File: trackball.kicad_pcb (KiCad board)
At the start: 2 copper layers, 27.5 x 35.2 mm, 37 parts, among them P1 CONN_10, P2 CONN_5, U1 MKL03Z32VFK4, U2 ADNS-3530, U4 ESD

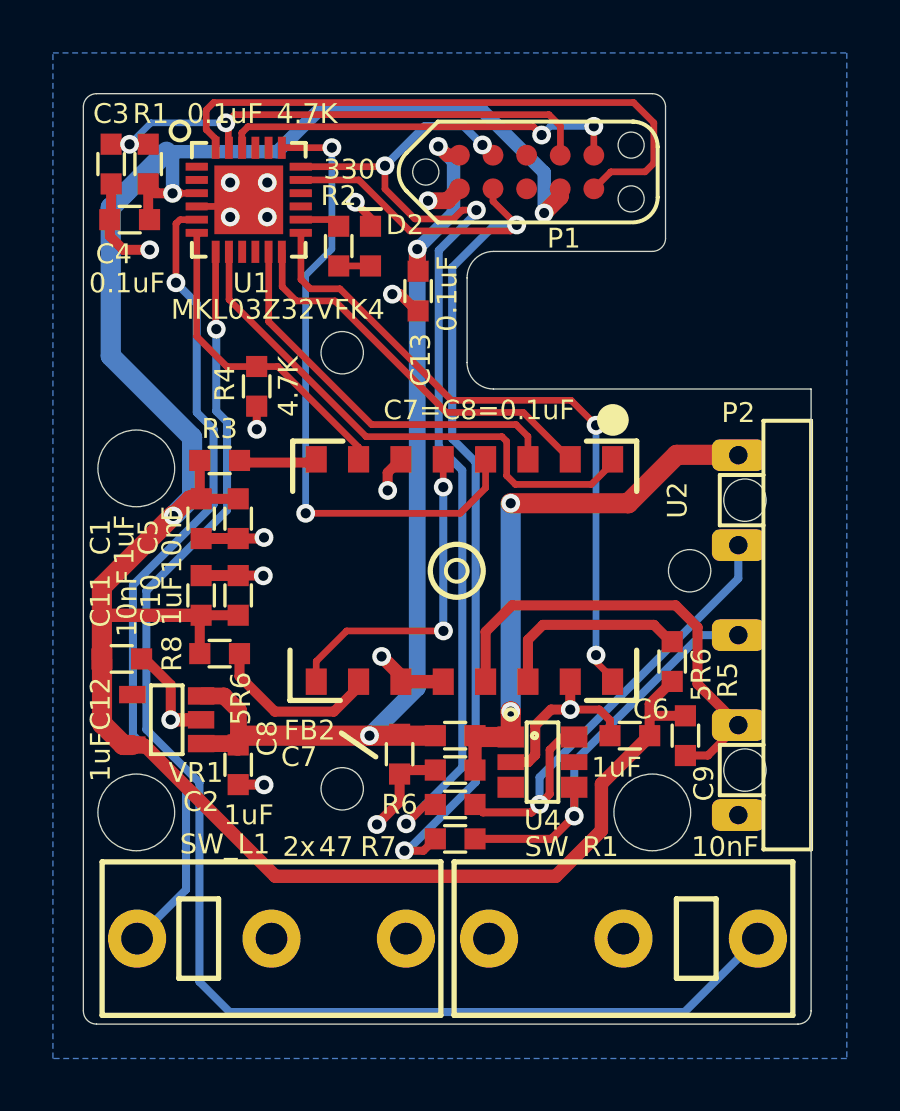
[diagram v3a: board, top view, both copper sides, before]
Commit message: Improve silk screen. Feature 5.6 instead of 5R6.
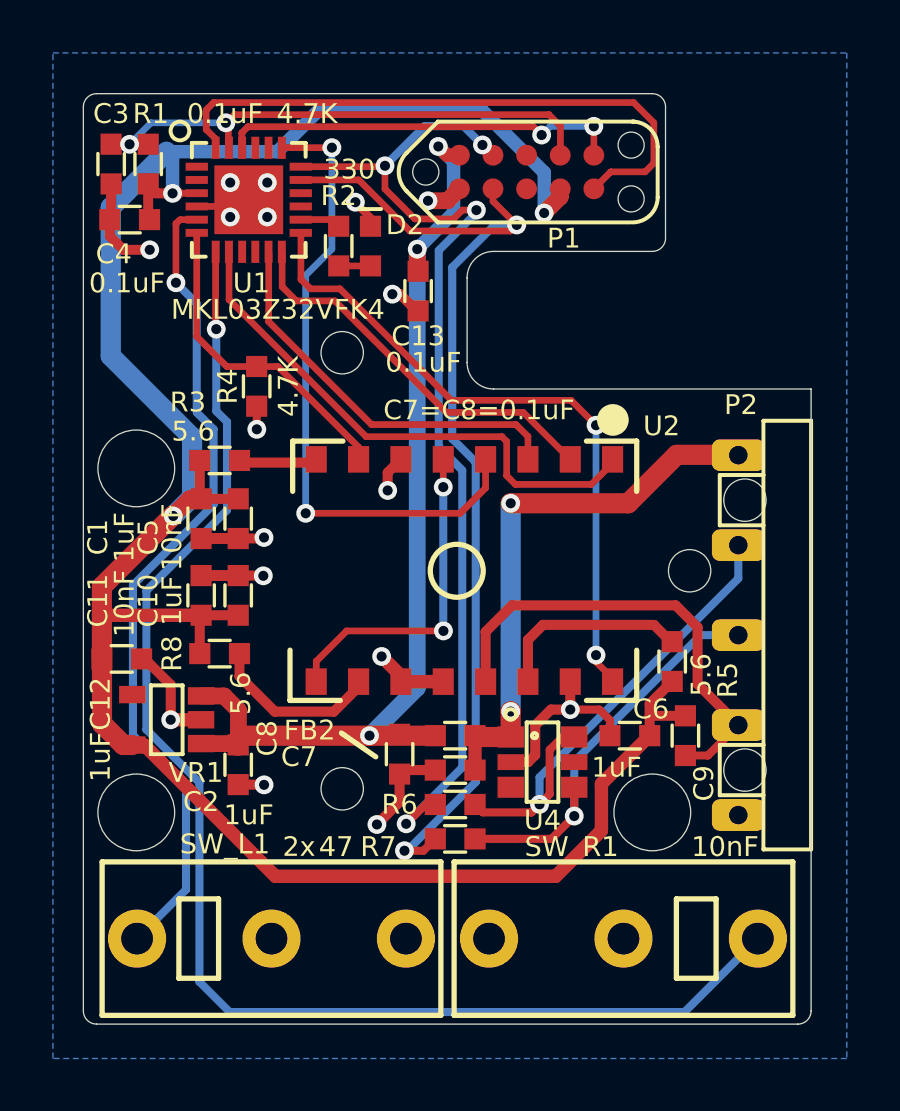
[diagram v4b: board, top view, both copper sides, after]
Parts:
- R3, R5, R8: value 5R6 -> 5.6
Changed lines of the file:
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@@
-(kicad_pcb (version 20171130) (host pcbnew 5.1.2-f72e74a~84~ubuntu18.04.1)
+(kicad_pcb (version 20171130) (host pcbnew 5.1.3-ffb9f22~84~ubuntu18.04.1)
   (general
     (thickness 1.6)
-    (drawings 43)
+    (drawings 42)
     (tracks 366)
     (zones 0)
@@
   (module ugl:ADNS-3530 locked (layer F.Cu)
     (at 196.260001 130.569003)
-    (fp_text reference U2 (at 8.339999 -2.669003 90) (layer F.SilkS)
+    (fp_text reference U2 (at 7.739999 -5.469003 180) (layer F.SilkS)
       (effects (font (size 0.746 0.746) (thickness 0.15)))
     )
@@
     (at 194.8 120 90)
     (attr smd)
-    (fp_text reference C13 (at -2.6 0.1 90) (layer F.SilkS)
-      (effects (font (size 0.75 0.75) (thickness 0.15)))
-    )
-    (fp_text value 0.1uF (at -0.1 1.1 90) (layer F.SilkS)
+    (fp_text reference C13 (at -1.7 0 180) (layer F.SilkS)
+      (effects (font (size 0.75 0.75) (thickness 0.15)))
+    )
+    (fp_text value 0.1uF (at -2.7 0.2 180) (layer F.SilkS)
       (effects (font (size 0.75 0.75) (thickness 0.15)))
     )
@@
     (at 186.6 131.5 270)
     (attr smd)
-    (fp_text reference C11 (at 0.2 3.8 270) (layer F.SilkS)
-      (effects (font (size 0.75 0.75) (thickness 0.15)))
-    )
-    (fp_text value 10nF (at 0.3 2.8 270) (layer F.SilkS)
+    (fp_text reference C11 (at 0.2 3.9 270) (layer F.SilkS)
+      (effects (font (size 0.75 0.75) (thickness 0.15)))
+    )
+    (fp_text value 10nF (at 0.3 2.9 270) (layer F.SilkS)
       (effects (font (size 0.75 0.75) (thickness 0.15)))
     )
@@
     (at 188 131.5 270)
     (attr smd)
-    (fp_text reference C10 (at 0.2 3.3 270) (layer F.SilkS)
+    (fp_text reference C10 (at 0.2 3.4 270) (layer F.SilkS)
       (effects (font (size 0.75 0.75) (thickness 0.15)))
     )
@@
     (at 187.3 126.4 180)
     (attr smd)
-    (fp_text reference R3 (at 0 1.2 180) (layer F.SilkS)
-      (effects (font (size 0.75 0.75) (thickness 0.15)))
-    )
-    (fp_text value 5R6 (at 0 1.5 180) (layer F.SilkS) hide
+    (fp_text reference R3 (at 1.2 2.2 180) (layer F.SilkS)
+      (effects (font (size 0.75 0.75) (thickness 0.15)))
+    )
+    (fp_text value 5.6 (at 1 1.1 180) (layer F.SilkS)
       (effects (font (size 0.75 0.75) (thickness 0.15)))
     )
@@
     (at 188.7 123.6 270)
     (attr smd)
-    (fp_text reference R4 (at -0.1 1.2 270) (layer F.SilkS)
+    (fp_text reference R4 (at 0 1.1 270) (layer F.SilkS)
       (effects (font (size 0.75 0.75) (thickness 0.15)))
     )
@@
       (effects (font (size 0.75 0.75) (thickness 0.15)))
     )
-    (fp_text value 5R6 (at 0.5 -1.1 90) (layer F.SilkS)
+    (fp_text value 5.6 (at 0.5 -1.1 90) (layer F.SilkS)
       (effects (font (size 0.75 0.75) (thickness 0.15)))
     )
@@
       (effects (font (size 0.75 0.75) (thickness 0.15)))
     )
-    (fp_text value 5R6 (at -0.8 -1.7 270) (layer F.SilkS)
+    (fp_text value 5.6 (at -0.8 -1.5 270) (layer F.SilkS)
       (effects (font (size 0.75 0.75) (thickness 0.15)))
     )
@@
     (at 186.6 128.6 90)
     (attr smd)
-    (fp_text reference C1 (at -0.7 -3.8 90) (layer F.SilkS)
-      (effects (font (size 0.75 0.75) (thickness 0.15)))
-    )
-    (fp_text value 1uF (at -0.8 -2.9 90) (layer F.SilkS)
+    (fp_text reference C1 (at -0.7 -3.9 90) (layer F.SilkS)
+      (effects (font (size 0.75 0.75) (thickness 0.15)))
+    )
+    (fp_text value 1uF (at -0.7 -2.9 90) (layer F.SilkS)
       (effects (font (size 0.75 0.75) (thickness 0.15)))
     )
@@
       (effects (font (size 0.75 0.75) (thickness 0.15)))
     )
-    (fp_text value 10nF (at -0.8 -2.5 90) (layer F.SilkS)
+    (fp_text value 10nF (at -0.7 -2.5 90) (layer F.SilkS)
       (effects (font (size 0.75 0.75) (thickness 0.15)))
     )
@@
     (at 209.65 133.000003)
     (attr virtual)
-    (fp_text reference P2 (at -2.75 -8.400003) (layer F.SilkS)
+    (fp_text reference P2 (at -2.65 -8.700003) (layer F.SilkS)
       (effects (font (size 0.75 0.75) (thickness 0.15)))
     )
@@
     (effects (font (size 0.75 0.75) (thickness 0.15)) (justify mirror))
   )
-  (gr_circle (center 196.260001 130.569003) (end 196.672312 130.569003) (layer F.SilkS) (width 0.15))
   (gr_circle (center 184.15 139.7) (end 184.15 141.35) (layer Eco1.User) (width 0.01))
   (gr_circle (center 191.931586 138.808826) (end 191.931586 140.308826) (layer Eco1.User) (width 0.01))

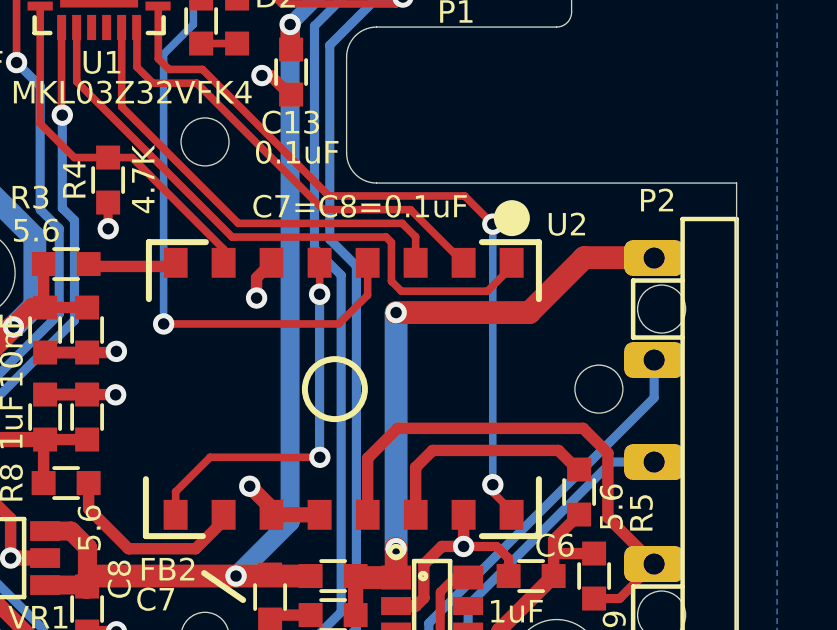
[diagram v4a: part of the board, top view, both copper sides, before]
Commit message: Update ADNS-3530 footprint.
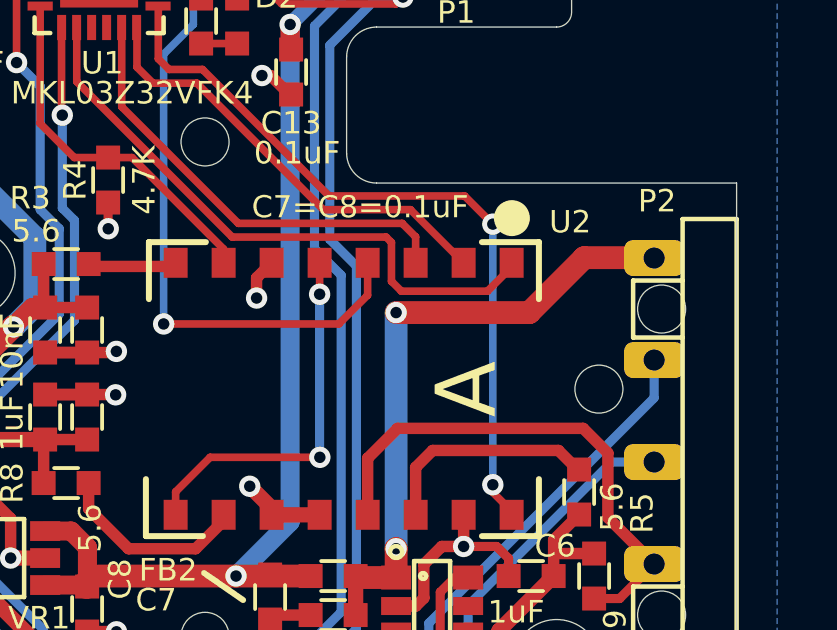
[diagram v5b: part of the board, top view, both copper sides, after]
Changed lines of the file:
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@@
     (add_net "Net-(VR1-Pad4)")
+  )
+  (module ugl:ADNS-3530 locked (layer F.Cu)
+    (at 196.260001 130.569003)
+    (fp_text reference U2 (at 7.839999 -5.569003 180) (layer F.SilkS)
+      (effects (font (size 0.746 0.746) (thickness 0.15)))
+    )
+    (fp_text value ADNS-3530 (at -3.206242 7.484879) (layer F.Fab)
+      (effects (font (size 1 1) (thickness 0.15)))
+    )
+    (fp_line (start -6.2 -4.9) (end -4.3 -4.9) (layer F.SilkS) (width 0.2))
+    (fp_line (start -6.2 -4.9) (end -6.2 -3) (layer F.SilkS) (width 0.2))
+    (fp_line (start -6.3 4.9) (end -4.4 4.9) (layer F.SilkS) (width 0.2))
+    (fp_line (start -6.3 4.9) (end -6.3 3) (layer F.SilkS) (width 0.2))
+    (fp_line (start 6.8 -4.9) (end 4.9 -4.9) (layer F.SilkS) (width 0.2))
+    (fp_line (start 6.8 -4.9) (end 6.8 -3) (layer F.SilkS) (width 0.2))
+    (fp_line (start 6.8 4.9) (end 6.8 3) (layer F.SilkS) (width 0.2))
+    (fp_line (start 6.8 4.9) (end 4.9 4.9) (layer F.SilkS) (width 0.2))
+    (fp_circle (center 5.9 -5.7) (end 6.2 -5.7) (layer F.SilkS) (width 0.6))
+    (fp_text user A (at 4.4 0 90) (layer F.SilkS)
+      (effects (font (size 2 2) (thickness 0.3)))
+    )
+    (pad 8 smd rect (at -5.31 -4.21) (size 0.8 1) (layers F.Cu F.Paste F.Mask)
+      (net 7 "Net-(R3-Pad1)"))
+    (pad 7 smd rect (at -3.71 -4.21) (size 0.8 1) (layers F.Cu F.Paste F.Mask)
+      (net 8 /SHTDWN))
+    (pad 6 smd rect (at -2.11 -4.21) (size 0.8 1) (layers F.Cu F.Paste F.Mask)
+      (net 1 GND))
+    (pad 5 smd rect (at -0.51 -4.21) (size 0.8 1) (layers F.Cu F.Paste F.Mask)
+      (net 9 "Net-(U2-Pad5)"))
+    (pad 4 smd rect (at 1.09 -4.21) (size 0.8 1) (layers F.Cu F.Paste F.Mask)
+      (net 10 /MOTION))
+    (pad 3 smd rect (at 2.69 -4.21) (size 0.8 1) (layers F.Cu F.Paste F.Mask)
+      (net 11 /MOSI))
+    (pad 2 smd rect (at 4.29 -4.21) (size 0.8 1) (layers F.Cu F.Paste F.Mask)
+      (net 12 /SCK))
+    (pad 1 smd rect (at 5.89 -4.21) (size 0.8 1) (layers F.Cu F.Paste F.Mask)
+      (net 13 /MISO))
+    (pad 9 smd rect (at -5.31 4.19) (size 0.8 1) (layers F.Cu F.Paste F.Mask)
+      (net 9 "Net-(U2-Pad5)"))
+    (pad 10 smd rect (at -3.71 4.19) (size 0.8 1) (layers F.Cu F.Paste F.Mask)
+      (net 14 "Net-(R8-Pad1)"))
+    (pad 11 smd rect (at -2.11 4.19) (size 0.8 1) (layers F.Cu F.Paste F.Mask)
+      (net 1 GND))
+    (pad 12 smd rect (at -0.51 4.19) (size 0.8 1) (layers F.Cu F.Paste F.Mask)
+      (net 1 GND))
+    (pad 13 smd rect (at 1.09 4.19) (size 0.8 1) (layers F.Cu F.Paste F.Mask)
+      (net 1 GND))
+    (pad 14 smd rect (at 2.69 4.19) (size 0.8 1) (layers F.Cu F.Paste F.Mask)
+      (net 15 "Net-(R5-Pad1)"))
+    (pad 15 smd rect (at 4.29 4.19) (size 0.8 1) (layers F.Cu F.Paste F.Mask)
+      (net 1 GND))
+    (pad 16 smd rect (at 5.89 4.19) (size 0.8 1) (layers F.Cu F.Paste F.Mask)
+      (net 16 /NCS))
   )
   (module ugl:CMI126603D08 locked (layer F.Cu)
@@
     (pad "" np_thru_hole circle (at 3.95 1.016) (size 0.98552 0.98552) (drill 0.98552) (layers *.Cu *.Mask F.SilkS))
   )
-  (module ugl:ADNS-3530 locked (layer F.Cu)
-    (at 196.260001 130.569003)
-    (fp_text reference U2 (at 7.739999 -5.469003 180) (layer F.SilkS)
-      (effects (font (size 0.746 0.746) (thickness 0.15)))
-    )
-    (fp_text value ADNS-3530 (at 0 6.7) (layer F.Fab)
-      (effects (font (size 1 1) (thickness 0.15)))
-    )
-    (fp_circle (center 5.9 -5.7) (end 6.2 -5.7) (layer F.SilkS) (width 0.6))
-    (fp_circle (center 0 0) (end 1 0) (layer F.SilkS) (width 0.2))
-    (fp_line (start 6.8 4.9) (end 4.9 4.9) (layer F.SilkS) (width 0.2))
-    (fp_line (start 6.8 4.9) (end 6.8 3) (layer F.SilkS) (width 0.2))
-    (fp_line (start 6.8 -4.9) (end 6.8 -3) (layer F.SilkS) (width 0.2))
-    (fp_line (start 6.8 -4.9) (end 4.9 -4.9) (layer F.SilkS) (width 0.2))
-    (fp_line (start -6.3 4.9) (end -6.3 3) (layer F.SilkS) (width 0.2))
-    (fp_line (start -6.3 4.9) (end -4.4 4.9) (layer F.SilkS) (width 0.2))
-    (fp_line (start -6.2 -4.9) (end -6.2 -3) (layer F.SilkS) (width 0.2))
-    (fp_line (start -6.2 -4.9) (end -4.3 -4.9) (layer F.SilkS) (width 0.2))
-    (pad 16 smd rect (at 5.89 4.19) (size 0.8 1) (layers F.Cu F.Paste F.Mask)
-      (net 16 /NCS))
-    (pad 15 smd rect (at 4.29 4.19) (size 0.8 1) (layers F.Cu F.Paste F.Mask)
-      (net 1 GND))
-    (pad 14 smd rect (at 2.69 4.19) (size 0.8 1) (layers F.Cu F.Paste F.Mask)
-      (net 15 "Net-(R5-Pad1)"))
-    (pad 13 smd rect (at 1.09 4.19) (size 0.8 1) (layers F.Cu F.Paste F.Mask)
-      (net 1 GND))
-    (pad 12 smd rect (at -0.51 4.19) (size 0.8 1) (layers F.Cu F.Paste F.Mask)
-      (net 1 GND))
-    (pad 11 smd rect (at -2.11 4.19) (size 0.8 1) (layers F.Cu F.Paste F.Mask)
-      (net 1 GND))
-    (pad 10 smd rect (at -3.71 4.19) (size 0.8 1) (layers F.Cu F.Paste F.Mask)
-      (net 14 "Net-(R8-Pad1)"))
-    (pad 9 smd rect (at -5.31 4.19) (size 0.8 1) (layers F.Cu F.Paste F.Mask)
-      (net 9 "Net-(U2-Pad5)"))
-    (pad 1 smd rect (at 5.89 -4.21) (size 0.8 1) (layers F.Cu F.Paste F.Mask)
-      (net 13 /MISO))
-    (pad 2 smd rect (at 4.29 -4.21) (size 0.8 1) (layers F.Cu F.Paste F.Mask)
-      (net 12 /SCK))
-    (pad 3 smd rect (at 2.69 -4.21) (size 0.8 1) (layers F.Cu F.Paste F.Mask)
-      (net 11 /MOSI))
-    (pad 4 smd rect (at 1.09 -4.21) (size 0.8 1) (layers F.Cu F.Paste F.Mask)
-      (net 10 /MOTION))
-    (pad 5 smd rect (at -0.51 -4.21) (size 0.8 1) (layers F.Cu F.Paste F.Mask)
-      (net 9 "Net-(U2-Pad5)"))
-    (pad 6 smd rect (at -2.11 -4.21) (size 0.8 1) (layers F.Cu F.Paste F.Mask)
-      (net 1 GND))
-    (pad 7 smd rect (at -3.71 -4.21) (size 0.8 1) (layers F.Cu F.Paste F.Mask)
-      (net 8 /SHTDWN))
-    (pad 8 smd rect (at -5.31 -4.21) (size 0.8 1) (layers F.Cu F.Paste F.Mask)
-      (net 7 "Net-(R3-Pad1)"))
-  )
   (module ugl:SM0603 (layer F.Cu)

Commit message: Bump version number to 1.0.0
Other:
- board text added: "PCB ID: trackball_main_1.0.0"
- board text removed: "PCB ID: trackball_main_0.1.0"
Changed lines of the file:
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@@
   (title_block
     (title "UHK Trackball Module")
-    (rev 0.1.0)
+    (rev 1.0.0)
     (company "Ultimate Gadget Laboratories Kft.")
   )
@@
     (effects (font (size 0.738 0.738) (thickness 0.15148)))
   )
-  (gr_text "PCB ID: trackball_main_0.1.0" (at 195.9 146.8) (layer B.SilkS)
+  (gr_text "PCB ID: trackball_main_1.0.0" (at 195.9 146.8) (layer B.SilkS)
     (effects (font (size 0.75 0.75) (thickness 0.15)) (justify mirror))
   )

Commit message: Make microswitch values consistent for them to show up as similar BOM components.
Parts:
- SW_L1: value MLK -> CMI126603D08
- SW_R1: value MRK -> CMI126603D08
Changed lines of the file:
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@@
       (effects (font (size 0.75 0.75) (thickness 0.15)))
     )
-    (fp_text value MRK (at 0 3.9) (layer F.Fab)
+    (fp_text value CMI126603D08 (at 0 3.9) (layer F.Fab)
       (effects (font (size 0.75 0.75) (thickness 0.15)))
     )
@@
       (effects (font (size 0.75 0.75) (thickness 0.15)))
     )
-    (fp_text value MLK (at 0 3.9) (layer F.Fab)
+    (fp_text value CMI126603D08 (at 0 3.9) (layer F.Fab)
       (effects (font (size 0.75 0.75) (thickness 0.15)))
     )
